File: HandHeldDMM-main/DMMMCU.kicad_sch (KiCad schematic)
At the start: 23 parts, among them IC1 REF35300QDBVR, J1 Conn_02x03_Odd_Even, J3 Conn_01x03, J4 Conn_02x05_Odd_Even, SW1 SW_Push, U7 STM32F373CCTx, Y1 16Mhz

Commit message: PCB rev 1 with schematic change ideas
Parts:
- added C27, C30, C35: 100nF, Capacitor_SMD:C_0402_1005Metric_Pad0.74x0.62mm_HandSolder, symbol Device:C
- added SW2, SW3, SW4: SW_Push, Button_Switch_SMD:SW_SPST_B3S-1000, symbol Switch:SW_Push
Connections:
- net GND: now also C27.2, C30.2, C35.2, SW2.2, SW3.2, SW4.2
- net VButton: now reaches U7.2 (PC13)
- net VButton: now also C27.1, SW2.1
- net CButton: now reaches U7.3 (PC14)
- net CButton: now also C30.1, SW3.1
- net RButton: now reaches U7.4 (PC15)
- net RButton: now also C35.1, SW4.1
- no-connect marks 10 -> 7
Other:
- note added: "Current Button"
- note added: "Resistance Button"
- note added: "Volts Button"
- moved on the sheet: C1, C2, C3, SW1, Y1

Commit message: Its going
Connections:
- net GPIO_17: now reaches U7.39 (PB3)
- net GPIO_16: now reaches U7.41 (PB5)
- no-connect marks 7 -> 5
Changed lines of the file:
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@@
   (junction (at 69.215 31.115) (diameter 0) (color 0 0 0 0)
   )
-  (no_connect (at 75.565 93.345))
-  (no_connect (at 75.565 98.425))
   (no_connect (at 75.565 90.805))
   (no_connect (at 259.715 36.83))
@@
     (stroke (width 0) (type default))
   )
+  (wire (pts (xy 75.565 93.345) (xy 80.01 93.345))
+    (stroke (width 0) (type default))
+  )
   (wire (pts (xy 55.245 37.465) (xy 55.245 40.005))
     (stroke (width 0) (type default))
@@
   )
   (wire (pts (xy 75.565 73.025) (xy 80.01 73.025))
+    (stroke (width 0) (type default))
+  )
+  (wire (pts (xy 75.565 98.425) (xy 80.01 98.425))
     (stroke (width 0) (type default))
   )
@@
     )
   )
+  (global_label "GPIO_17" (shape input) (at 80.01 93.345 0) (fields_autoplaced)
+    (effects (font (size 1.27 1.27)) (justify left))
+    (property "Intersheetrefs" "${INTERSHEET_REFS}" (at 90.8571 93.345 0)
+      (effects (font (size 1.27 1.27)) (justify left) hide)
+    )
+  )
+  (global_label "GPIO_16" (shape input) (at 80.01 98.425 0) (fields_autoplaced)
+    (effects (font (size 1.27 1.27)) (justify left))
+    (property "Intersheetrefs" "${INTERSHEET_REFS}" (at 90.8571 98.425 0)
+      (effects (font (size 1.27 1.27)) (justify left) hide)
+    )
+  )

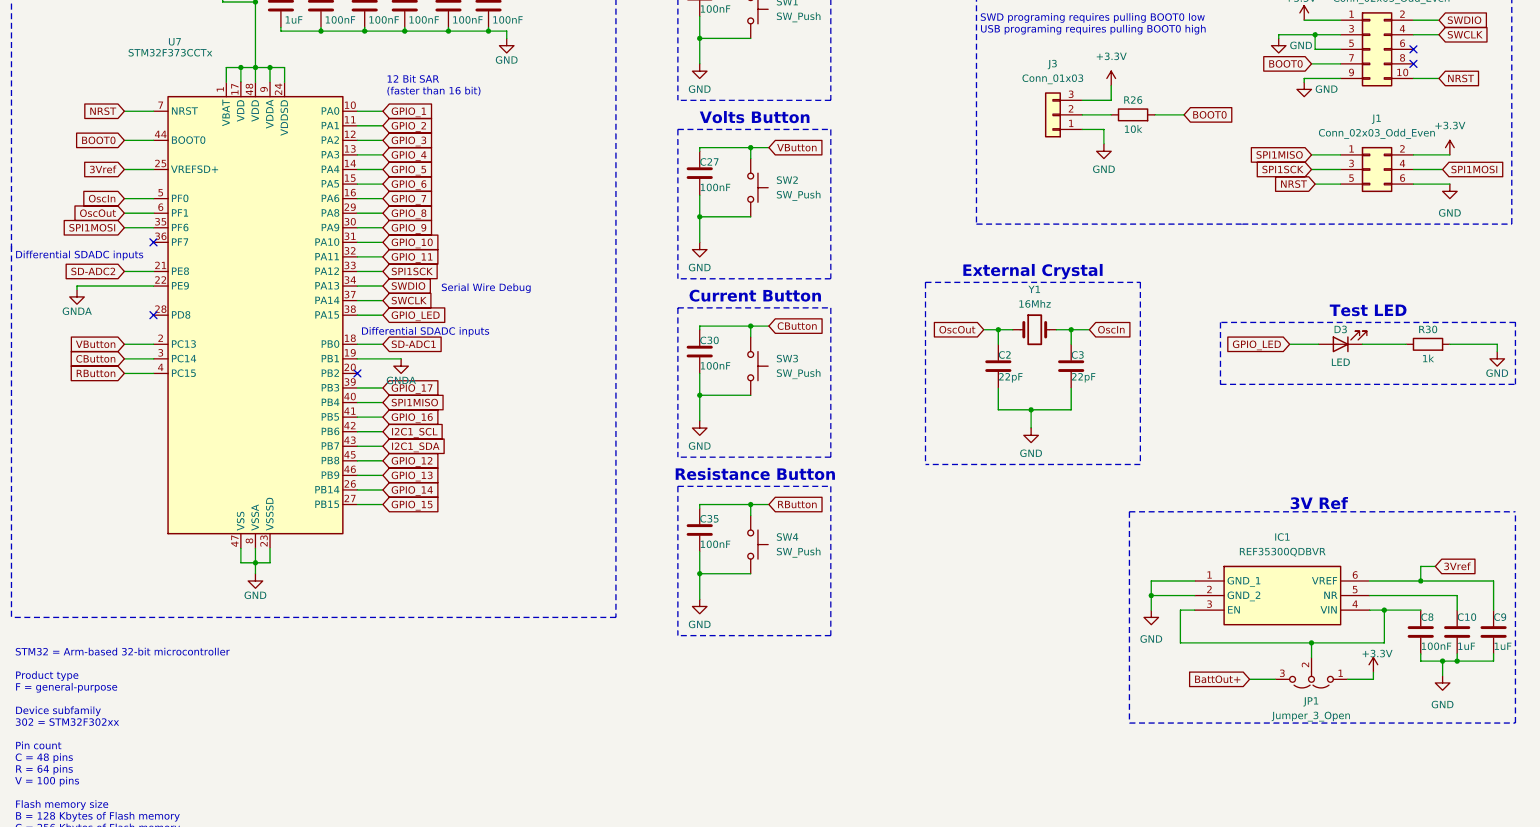
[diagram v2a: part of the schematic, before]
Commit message: Layout / routing V2 with schematic fixes
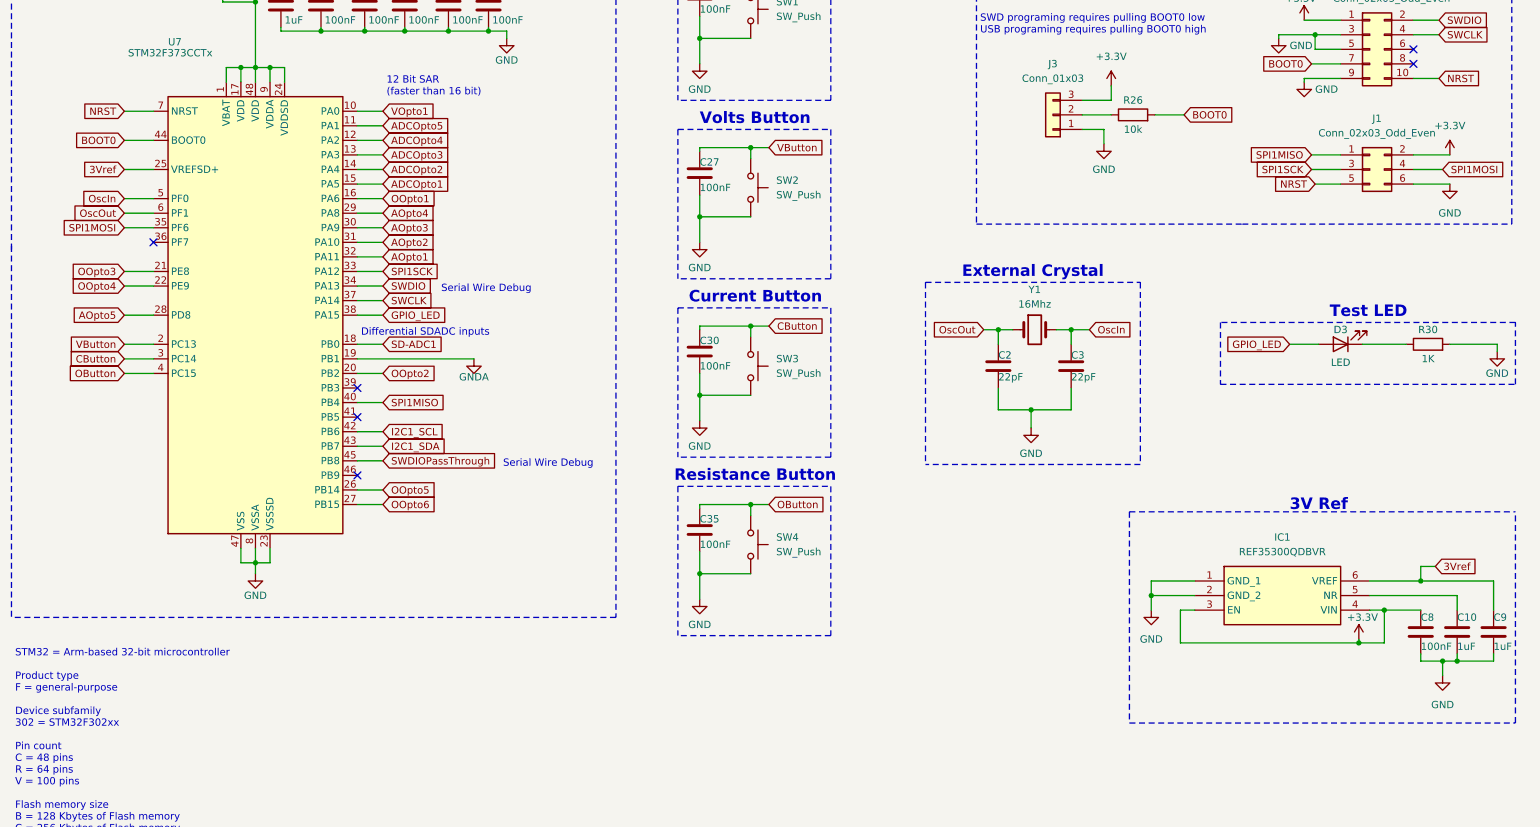
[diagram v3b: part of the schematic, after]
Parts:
- removed JP1: Jumper_3_Open, Jumper:SolderJumper-3_P1.3mm_Open_RoundedPad1.0x1.5mm_NumberLabels, symbol Jumper:Jumper_3_Open
- C1, C27, C29, C30, C31, C32, C33, C34, C35, C8: LCSC Price 0 -> 0.18; PART# (none) -> C513772; Price / 1 (none) -> 0.0018; Price Qty 0 -> 100; Store Parts Bin -> https://www.lcsc.com/product-detail/Multilayer-Ceramic-Capa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
- C10, C26, C9: PART# (none) -> C14445; Price / 1 (none) -> 0.0017
- IC1: Height 1.45 -> (none); Manufacturer_Name Texas Instruments -> (none); Manufacturer_Part_Number REF35300QDBVR -> (none); Mouser Part Number 595-REF35300QDBVR -> (none); Mouser Price/Stock https://www.mouser.co.uk/ProductDetail/Texas-Instruments/RE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 -> (none); PART# (none) -> C6643299; Price / 1 (none) -> 3.0896
- R26: PART# (none) -> C103199; Price / 1 (none) -> 0.001
- R30: value 1k -> 1K; PART# (none) -> C5141145; Price / 1 (none) -> 0.0049
- SW1, SW2, SW3, SW4: PART# (none) -> C2888900; Price / 1 (none) -> 0.0079
- U7: PART# (none) -> C89403; Price / 1 (none) -> 5.067
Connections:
- net +3.3V: now also C8.1, IC1.3 (EN), IC1.4 (VIN)
- net GNDA: no longer U7.22 (PE9)
- net OOpto2: now reaches U7.20 (PB2)
- net AOpto5: now reaches U7.28 (PD8)
- net GPIO_1 renamed VOpto1
- net GPIO_10 renamed AOpto2
- net GPIO_11 renamed AOpto1
- net GPIO_12 renamed SWDIOPassThrough
- net GPIO_13: no longer names the net of U7.46 (PB9)
- net GPIO_14 renamed OOpto5
- net GPIO_15 renamed OOpto6
- net GPIO_16: no longer names the net of U7.41 (PB5)
- net GPIO_17: no longer names the net of U7.39 (PB3)
- net GPIO_2 renamed ADCOpto5
- net GPIO_3 renamed ADCOpto4
- net GPIO_4 renamed ADCOpto3
- net GPIO_5 renamed ADCOpto2
- net GPIO_6 renamed ADCOpto1
- net GPIO_7 renamed OOpto1
- net GPIO_8 renamed AOpto4
- net GPIO_9 renamed AOpto3
- net RButton renamed OButton
- net SD-ADC2 renamed OOpto3
- new net OOpto4: U7.22 (PE9)
- no-connect marks 5 -> 6

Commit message: Finished?
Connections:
- net SWDIOPassThrough is gone; now on net SWDIO: U7.45 (PB8)
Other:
- note added: "Serial Wire Debug Pass Through"
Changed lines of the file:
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@@
     (effects (font (size 1.27 1.27)) (justify left bottom))
   )
-  (text "Serial Wire Debug" (at 100.965 107.315 0)
+  (text "Serial Wire Debug Pass Through" (at 88.9 107.315 0)
     (effects (font (size 1.27 1.27)) (justify left bottom))
   )
@@
     )
   )
+  (global_label "SWDIO" (shape input) (at 80.01 106.045 0) (fields_autoplaced)
+    (effects (font (size 1.27 1.27)) (justify left))
+    (property "Intersheetrefs" "${INTERSHEET_REFS}" (at 88.8614 106.045 0)
+      (effects (font (size 1.27 1.27)) (justify left) hide)
+    )
+  )
   (global_label "GPIO_LED" (shape input) (at 80.01 80.645 0) (fields_autoplaced)
     (effects (font (size 1.27 1.27)) (justify left))
@@
       (effects (font (size 1.27 1.27)) (justify left) hide)
     )
-  )
-  (global_label "SWDIOPassThrough" (shape input) (at 80.01 106.045 0) (fields_autoplaced)
-    (effects (font (size 1.27 1.27)) (justify left))
-    (property "Intersheetrefs" "${INTERSHEET_REFS}" (at 100.8354 106.045 0)
-      (effects (font (size 1.27 1.27)) (justify left) hide)
-    )

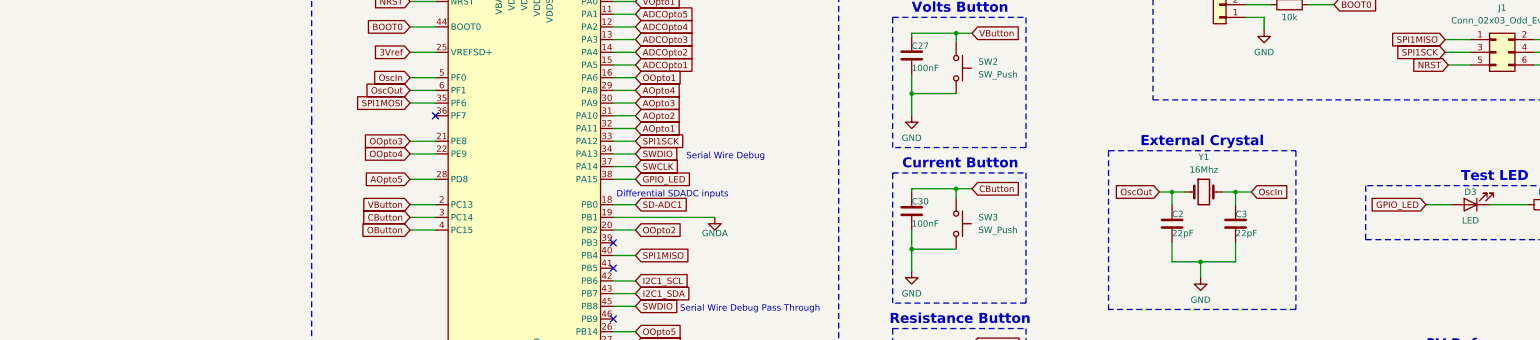
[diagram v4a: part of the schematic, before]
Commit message: NOT BIPOLAR ADC YOU DUMBASS!!!!
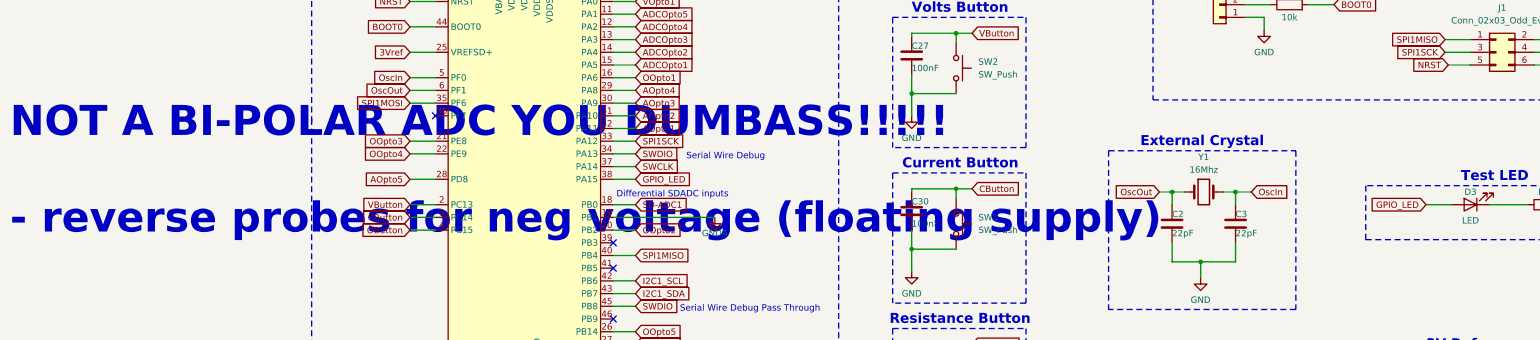
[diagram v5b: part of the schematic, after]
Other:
- note added: "NOT A BI-POLAR ADC YOU DUMBASS!!!!! - reverse probes for neg voltage (floating supply)"
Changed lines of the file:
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@@
     (effects (font (size 2 2) (thickness 0.4) bold) (justify left bottom))
+  )
+  (text "NOT A BI-POLAR ADC YOU DUMBASS!!!!!\n\n- reverse probes for neg voltage (floating supply)"
+    (at -45.085 92.075 0)
+    (effects (font (size 6 6) (thickness 1.2) bold) (justify left bottom))
   )
   (text "STM32 MCU" (at 52.07 16.51 0)
